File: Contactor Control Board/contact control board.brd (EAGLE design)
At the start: 63.2 x 38.1 mm, 30 parts, among them Q4 MOSFET-NCHANNELFQP30N06L

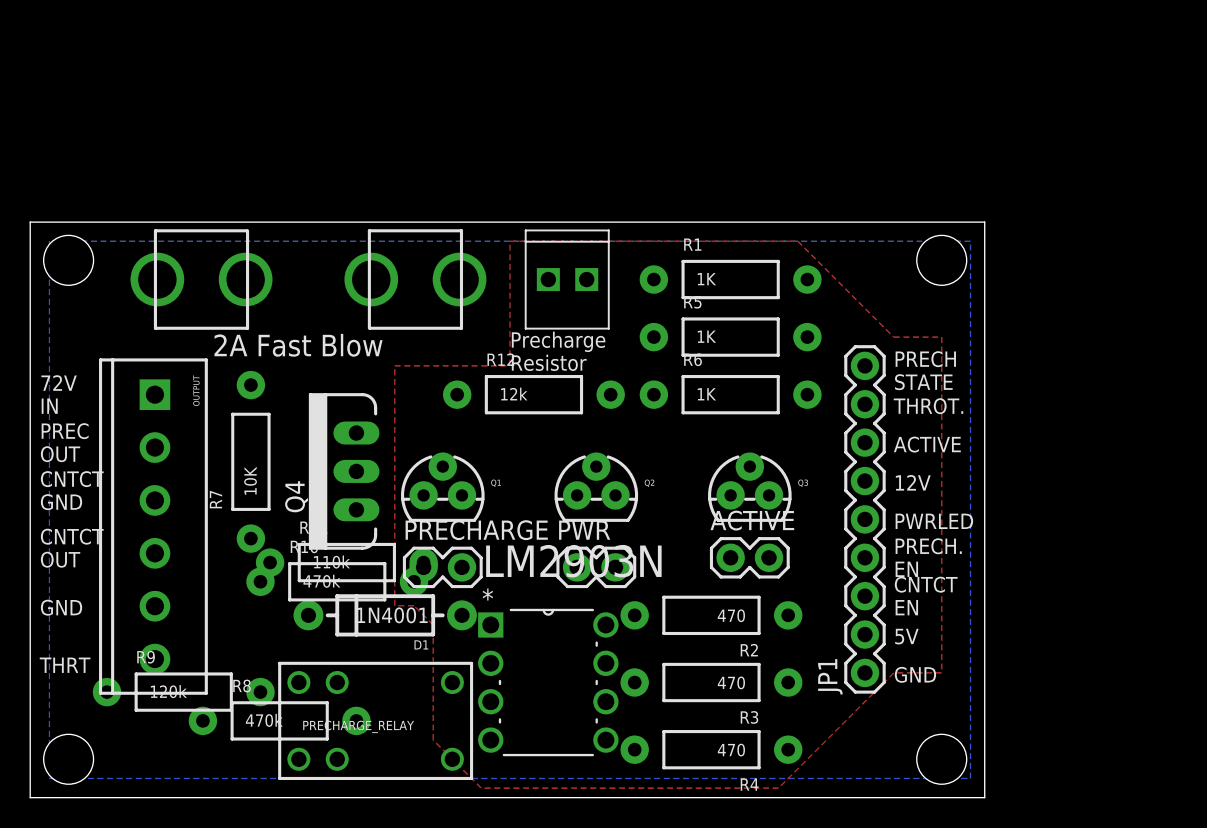
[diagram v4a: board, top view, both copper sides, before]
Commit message: Final draft design for CCB (thru-hole) before proto-boarding.
Replaced SPST relay with DPDT relay so that its NC connections will
drain the capacitors and its NO connections will charge them. This way
we can wait a shorter period of time after powering down the machine
before servicing!
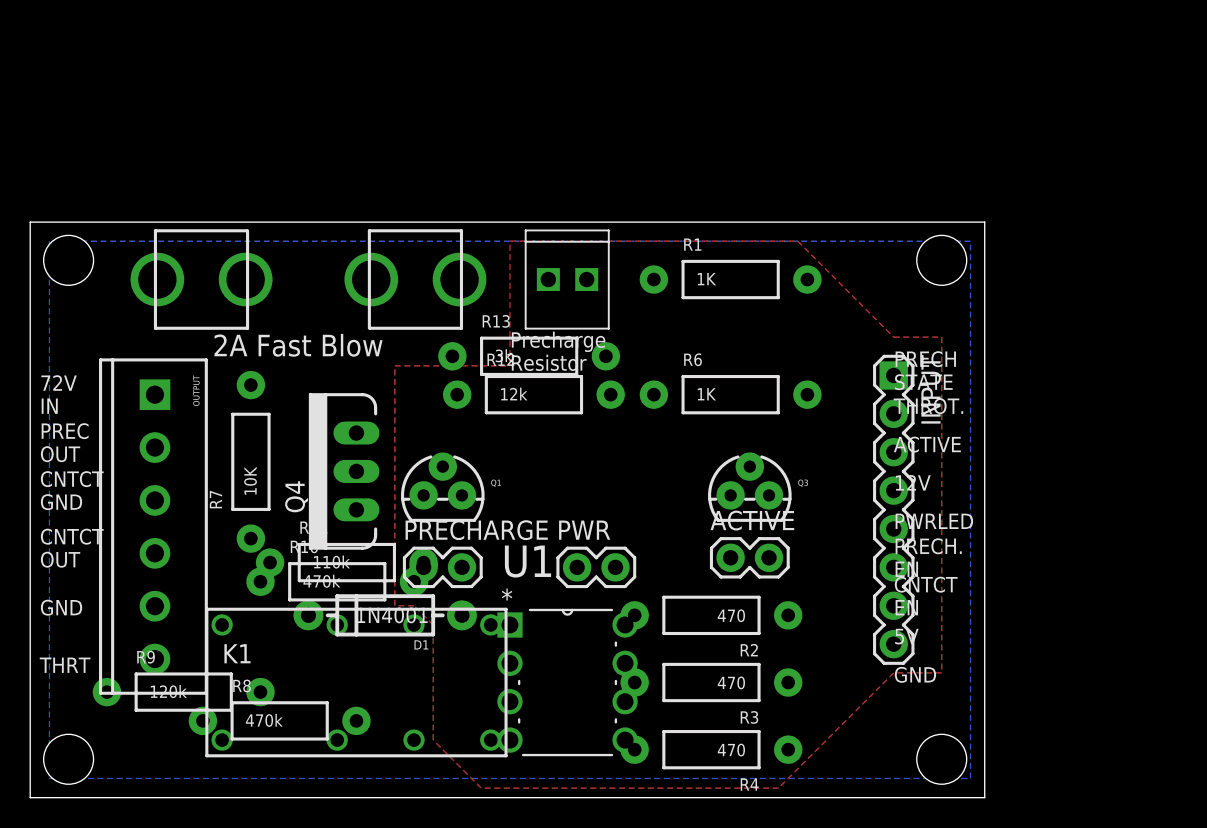
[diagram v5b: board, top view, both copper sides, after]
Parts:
- removed JP1: M09, SparkFun-Connectors:1X09
- removed LM2903N: LM2903N, Fairchild_By_element14_Batch_1:DIP254P762X508-8
- removed PRECHARGE_RELAY: RELAY-2G5Q, SparkFun-Electromechanical:RELAY-G5V
- removed Q2: (no value), SparkFun-DiscreteSemi:TO-92
- removed R5: 1K, SparkFun-Resistors:AXIAL-0.4
- added INPUT: (no value), SparkFun-Connectors:1X08
- added K1: DS2Y-S-DC5V, relay:DS2Y
- added R13: 3k, SparkFun-Resistors:AXIAL-0.4
- added U1: LM393AN, Fairchild_By_element14_Batch_1:DIP254P762X508-8
- Q1, Q3: value (none) -> 2n2222
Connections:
- removed net N$2: Q2.3, R3.P$2
- removed net PRECHARGE_INPUT: PRECHARGE_RELAY.5, PRECHARGE_RELAY.6, R9.P$2, RESISTOR.P2
- removed net PWR_LED: JP1.5, R5.P$1
- removed net PWR_TRAN_IN: Q2.2, R5.P$2
- new net PRECHARGE_RESISTOR_IN: K1.4, RESISTOR.P1
- new net PRECHARGE_RESISTOR_OUT: K1.13, R9.P$2, RESISTOR.P2
- net 12V: now also INPUT.5; no longer JP1.6
- net 5V: now also INPUT.2, K1.1, R13.P$1, U1.8; no longer JP1.2, LM2903N.8, PRECHARGE_RELAY.2
- net 72V_IN_FUSED: now also K1.8; no longer RESISTOR.P1
- net ACTIVE_LED_EN: now also INPUT.6; no longer JP1.7
- net CAP_CHARGE_REF: now also U1.2
- net CAP_CHARGE_V_CURR: now also U1.3
- net CONTACT_EN: now also INPUT.3; no longer JP1.3
- net GND: now also INPUT.1, K1.11, R3.P$2, U1.4; no longer JP1.1, LM2903N.4, Q2.1
- net PRECHARGE_EN: now also INPUT.4; no longer JP1.4
- net PRECHARGE_OUT: now also K1.6, K1.9; no longer PRECHARGE_RELAY.10
- net PRECH_STATE: now also INPUT.8, R13.P$2, U1.1; no longer JP1.9, LM2903N.1
- net PRECH_TRAN_COLLECTOR: now also K1.16; no longer PRECHARGE_RELAY.9
- net THROTTLE: now also INPUT.7; no longer JP1.8

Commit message: Simplified board by removing power LED pin, it's just run from 5V now.
Swapped pins in the voltage comparator to produce a HIGH output when the
capacitor voltage drops below the reference voltage (instead of vice
versa).
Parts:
- moved INPUT 19.8 mm to (55.2, 8.26), turned to 90 degrees
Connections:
- net ACTIVE_TRAN_IN renamed N$2
- net 72V_IN_FUSED: no longer R8.P$1
- net CAP_CHARGE_REF: now also U1.3; no longer U1.2
- net CAP_CHARGE_V_CURR: now also U1.2; no longer U1.3
- net PRECHARGE_RESISTOR_IN: now also R8.P$1
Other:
- board text added: "CNTCT +VE"
- board text removed: "CNTCT OUT"
- board text removed: "PWRLED"
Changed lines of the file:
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@@
 <setting verticaltext="up"/>
 </settings>
-<grid distance="0.05" unitdist="inch" unit="inch" style="lines" multiple="1" display="yes" altdistance="0.005" altunitdist="inch" altunit="inch"/>
+<grid distance="0.0125" unitdist="inch" unit="inch" style="lines" multiple="1" display="yes" altdistance="0.005" altunitdist="inch" altunit="inch"/>
 <layers>
 <layer number="1" name="Top" color="4" fill="1" visible="yes" active="yes"/>
@@
 <layer number="23" name="tOrigins" color="15" fill="1" visible="yes" active="yes"/>
 <layer number="24" name="bOrigins" color="15" fill="1" visible="yes" active="yes"/>
-<layer number="25" name="tNames" color="16" fill="1" visible="no" active="yes"/>
+<layer number="25" name="tNames" color="16" fill="1" visible="yes" active="yes"/>
 <layer number="26" name="bNames" color="16" fill="1" visible="no" active="yes"/>
 <layer number="27" name="tValues" color="7" fill="1" visible="no" active="yes"/>
@@
 GND</text>
 <text x="0.635" y="15.24" size="1.016" layer="25" font="vector" ratio="15">CNTCT
-OUT</text>
++VE</text>
 <text x="0.635" y="12.065" size="1.016" layer="25" font="vector" ratio="15">GND</text>
 <text x="0.635" y="8.255" size="1.016" layer="25" font="vector" ratio="15">THRT</text>
@@
 <text x="57.15" y="14.605" size="1.016" layer="25" font="vector" ratio="15">PRECH.
 EN</text>
-<text x="57.15" y="17.78" size="1.016" layer="25" font="vector" ratio="15">PWRLED</text>
-<text x="57.15" y="20.32" size="1.016" layer="25" font="vector" ratio="15">12V</text>
-<text x="57.15" y="22.86" size="1.016" layer="25" font="vector" ratio="15">ACTIVE</text>
-<text x="57.15" y="25.4" size="1.016" layer="25" font="vector" ratio="15">THROT.</text>
+<text x="57.15" y="17.78" size="1.016" layer="25" font="vector" ratio="15">12V</text>
+<text x="57.15" y="20.0025" size="1.016" layer="25" font="vector" ratio="15">ACTIVE</text>
+<text x="57.15" y="22.86" size="1.016" layer="25" font="vector" ratio="15">THROT.</text>
 <text x="31.75" y="28.2575" size="1.016" layer="25" font="vector" ratio="15">Precharge
 Resistor</text>
-<text x="57.15" y="26.9875" size="1.016" layer="25" font="vector" ratio="15">PRECH
+<text x="57.15" y="24.765" size="1.016" layer="25" font="vector" ratio="15">PRECH
 STATE</text>
 </plain>
@@
 <element name="R12" library="SparkFun-Resistors" package="AXIAL-0.4" value="12k" x="33.3375" y="26.67"/>
 <element name="R13" library="SparkFun-Resistors" package="AXIAL-0.4" value="3k" x="33.02" y="29.21"/>
-<element name="INPUT" library="SparkFun-Connectors" package="1X08" value="" x="57.15" y="27.94" rot="R270"/>
+<element name="INPUT" library="SparkFun-Connectors" package="1X08" value="" x="55.245" y="8.255" rot="R90"/>
 <element name="K1" library="relay" package="DS2Y" value="DS2Y-S-DC5V" x="21.59" y="7.62">
 <attribute name="OC_NEWARK" value="13P3268" x="21.59" y="7.62" size="1.778" layer="27" ratio="15" display="off"/>
@@
 <contactref element="K1" pad="1"/>
 <contactref element="U1" pad="8"/>
-<wire x1="46.355" y1="15.875" x2="57.15" y2="25.4" width="0" layer="19" extent="1-1"/>
+<wire x1="46.355" y1="15.875" x2="55.245" y2="10.795" width="0" layer="19" extent="1-1"/>
 <wire x1="36.195" y1="15.24" x2="46.355" y2="15.875" width="0" layer="19" extent="1-1"/>
 <wire x1="26.035" y1="15.24" x2="36.195" y2="15.24" width="0" layer="19" extent="1-1"/>
@@
 <contactref element="U1" pad="4"/>
 <contactref element="R3" pad="P$2"/>
-<wire x1="46.355" y1="20.0025" x2="57.15" y2="27.94" width="0" layer="19" extent="1-1"/>
+<wire x1="46.355" y1="20.0025" x2="55.245" y2="8.255" width="0" layer="19" extent="1-1"/>
 <wire x1="38.4175" y1="26.67" x2="46.355" y2="20.0025" width="0" layer="19" extent="1-1"/>
 <wire x1="40.005" y1="7.62" x2="46.355" y2="20.0025" width="0" layer="19" extent="1-1"/>
@@
 <contactref element="R7" pad="P$2"/>
 <contactref element="INPUT" pad="3"/>
-<wire x1="21.59" y1="19.05" x2="57.15" y2="22.86" width="0" layer="19" extent="1-1"/>
+<wire x1="21.59" y1="19.05" x2="55.245" y2="13.335" width="0" layer="19" extent="1-1"/>
 <wire x1="14.605" y1="27.305" x2="21.59" y2="19.05" width="0" layer="19" extent="1-1"/>
 </signal>
@@
 <contactref element="R6" pad="P$1"/>
 <contactref element="INPUT" pad="4"/>
-<wire x1="41.275" y1="26.67" x2="57.15" y2="20.32" width="0" layer="19" extent="1-1"/>
+<wire x1="41.275" y1="26.67" x2="55.245" y2="15.875" width="0" layer="19" extent="1-1"/>
 </signal>
 <signal name="12V">
 <contactref element="OUTPUT" pad="4"/>
 <contactref element="INPUT" pad="5"/>
-<wire x1="8.255" y1="16.17" x2="57.15" y2="17.78" width="0" layer="19" extent="1-1"/>
+<wire x1="8.255" y1="16.17" x2="55.245" y2="18.415" width="0" layer="19" extent="1-1"/>
 </signal>
 <signal name="ACTIVE_LED_EN">
 <contactref element="R1" pad="P$1"/>
 <contactref element="INPUT" pad="6"/>
-<wire x1="57.15" y1="15.24" x2="41.275" y2="34.29" width="0" layer="19" extent="1-1"/>
+<wire x1="55.245" y1="20.955" x2="41.275" y2="34.29" width="0" layer="19" extent="1-1"/>
 </signal>
 <signal name="THROTTLE">
 <contactref element="OUTPUT" pad="6"/>
 <contactref element="INPUT" pad="7"/>
-<wire x1="8.255" y1="9.17" x2="57.15" y2="12.7" width="0" layer="19" extent="1-1"/>
+<wire x1="8.255" y1="9.17" x2="55.245" y2="23.495" width="0" layer="19" extent="1-1"/>
 </signal>
 <signal name="72V_IN">
@@
 <contactref element="PRECHARGE_FUSE" pad="1"/>
 <contactref element="R10" pad="P$1"/>
-<contactref element="R8" pad="P$1"/>
 <contactref element="K1" pad="8"/>
 <wire x1="15.24" y1="14.2875" x2="28.415" y2="34.29" width="0" layer="19" extent="1-1"/>
-<wire x1="11.43" y1="5.08" x2="15.24" y2="14.2875" width="0" layer="19" extent="1-1"/>
-<wire x1="30.48" y1="3.81" x2="11.43" y2="5.08" width="0" layer="19" extent="1-1"/>
+<wire x1="30.48" y1="3.81" x2="15.24" y2="14.2875" width="0" layer="19" extent="1-1"/>
 </signal>
 <signal name="CONTACT_GND">
@@
 <contactref element="Q4" pad="2"/>
 <wire x1="8.255" y1="19.67" x2="21.59" y2="21.59" width="0" layer="19" extent="1-1"/>
-</signal>
-<signal name="ACTIVE_TRAN_IN">
-<contactref element="R1" pad="P$2"/>
-<contactref element="Q3" pad="2"/>
-<wire x1="47.625" y1="21.9075" x2="51.435" y2="34.29" width="0" layer="19" extent="1-1"/>
-</signal>
-<signal name="PRECH_TRAN_IN">
-<contactref element="R6" pad="P$2"/>
-<contactref element="Q1" pad="2"/>
-<wire x1="27.305" y1="21.9075" x2="51.435" y2="26.67" width="0" layer="19" extent="1-1"/>
 </signal>
 <signal name="N$1">
@@
 <contactref element="INPUT" pad="8"/>
 <contactref element="U1" pad="1"/>
-<wire x1="57.15" y1="10.16" x2="38.1" y2="29.21" width="0" layer="19" extent="1-1"/>
+<wire x1="55.245" y1="26.035" x2="38.1" y2="29.21" width="0" layer="19" extent="1-1"/>
 <wire x1="31.75" y1="11.43" x2="38.1" y2="29.21" width="0" layer="19" extent="1-1"/>
 </signal>
@@
 <contactref element="R11" pad="P$2"/>
 <contactref element="R12" pad="P$1"/>
-<contactref element="U1" pad="2"/>
+<contactref element="U1" pad="3"/>
 <wire x1="26.035" y1="15.5575" x2="28.2575" y2="26.67" width="0" layer="19" extent="1-1"/>
-<wire x1="31.75" y1="8.89" x2="26.035" y2="15.5575" width="0" layer="19" extent="1-1"/>
+<wire x1="31.75" y1="6.35" x2="26.035" y2="15.5575" width="0" layer="19" extent="1-1"/>
 </signal>
 <signal name="N$3">
@@
 <contactref element="R8" pad="P$2"/>
 <contactref element="R9" pad="P$1"/>
-<contactref element="U1" pad="3"/>
+<contactref element="U1" pad="2"/>
+<wire x1="21.59" y1="5.08" x2="31.75" y2="8.89" width="0" layer="19" extent="1-1"/>
 <wire x1="5.08" y1="6.985" x2="21.59" y2="5.08" width="0" layer="19" extent="1-1"/>
-<wire x1="31.75" y1="6.35" x2="5.08" y2="6.985" width="0" layer="19" extent="1-1"/>
 </signal>
 <signal name="PRECHARGE_RESISTOR_IN">
 <contactref element="RESISTOR" pad="P1"/>
 <contactref element="K1" pad="4"/>
+<contactref element="R8" pad="P$1"/>
 <wire x1="20.32" y1="3.81" x2="36.83" y2="34.29" width="0" layer="19" extent="1-1"/>
+<wire x1="11.43" y1="5.08" x2="20.32" y2="3.81" width="0" layer="19" extent="1-1"/>
 </signal>
 <signal name="PRECHARGE_RESISTOR_OUT">
@@
 <wire x1="15.24" y1="6.985" x2="20.32" y2="11.43" width="0" layer="19" extent="1-1"/>
 </signal>
+<signal name="N$2">
+<contactref element="R1" pad="P$2"/>
+<contactref element="Q3" pad="2"/>
+<wire x1="47.625" y1="21.9075" x2="51.435" y2="34.29" width="0" layer="19" extent="1-1"/>
+</signal>
+<signal name="PRECH_TRAN_IN">
+<contactref element="R6" pad="P$2"/>
+<contactref element="Q1" pad="2"/>
+<wire x1="27.305" y1="21.9075" x2="51.435" y2="26.67" width="0" layer="19" extent="1-1"/>
+</signal>
 </signals>

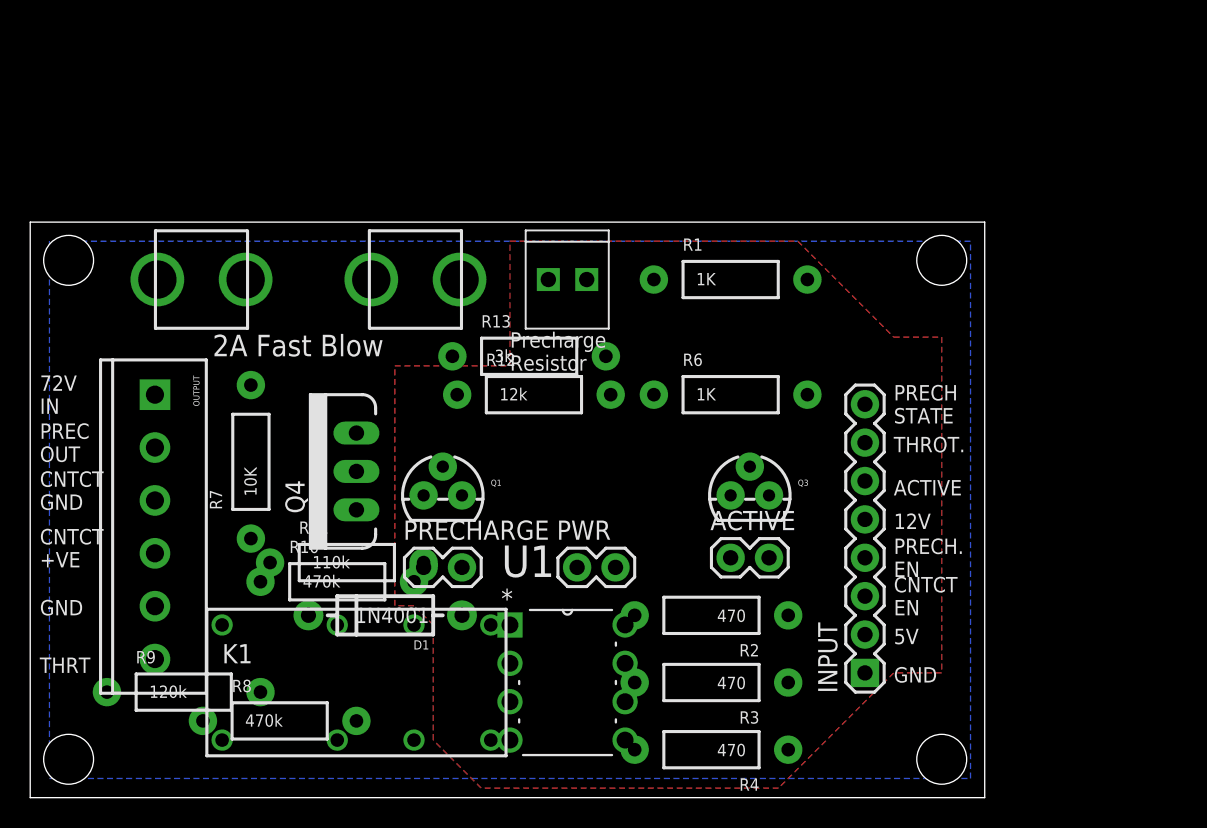
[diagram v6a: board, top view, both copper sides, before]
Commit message: Updating layout to 2"x3". Need to make smaller!
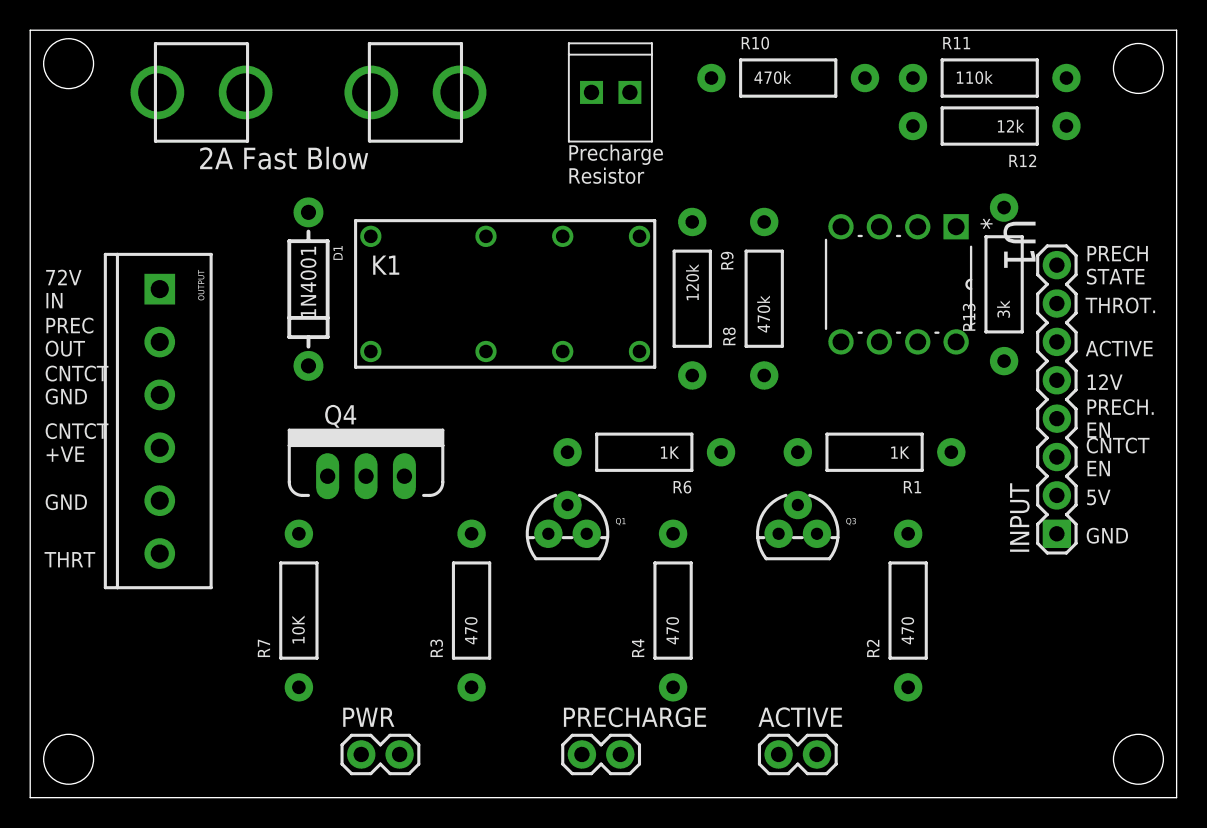
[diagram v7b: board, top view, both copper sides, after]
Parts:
- moved R11 53.3 mm to (63.5, 47.6)
- moved R10 44.7 mm to (50.2, 47.6)
- moved R9 42.5 mm to (43.8, 33.0), turned to 270 degrees
- moved R8 42.5 mm to (48.6, 33.0), turned to 90 degrees
- moved R12 35.0 mm to (63.5, 44.5), turned to 180 degrees
- moved R13 31.8 mm to (64.5, 34.0), turned to 90 degrees
- moved U1 30.0 mm to (53.7, 30.2), turned to 270 degrees
- moved K1 27.5 mm to (31.4, 33.3)
- moved D1 22.2 mm to (18.4, 33.7), turned to 270 degrees
- moved PWR 18.9 mm to (21.9, 2.86)
- moved STANDOFF3 18.2 mm to (73.3, 48.3)
- moved R3 16.6 mm to (29.2, 12.4), turned to 90 degrees
- moved PRECHARGE 16.2 mm to (36.5, 2.86)
- moved INPUT 15.7 mm to (67.9, 17.5)
- moved R1 14.9 mm to (55.9, 22.9), turned to 180 degrees
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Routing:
- removed copper zone on layer 1, net 5V
- removed copper zone on layer 16, net GND
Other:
- board size 63.2 x 38.1 mm -> 75.9 x 50.8 mm
